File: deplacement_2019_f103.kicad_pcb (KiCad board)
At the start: 2 copper layers, 67.3 x 80 mm, 17 parts, among them J1 alim_logique_5V, J2 moteur_droit, J3 moteur_gauche, J4 Conn_01x03, J5 QEI_droite, J6 QEI_gauche, U1 black_pill

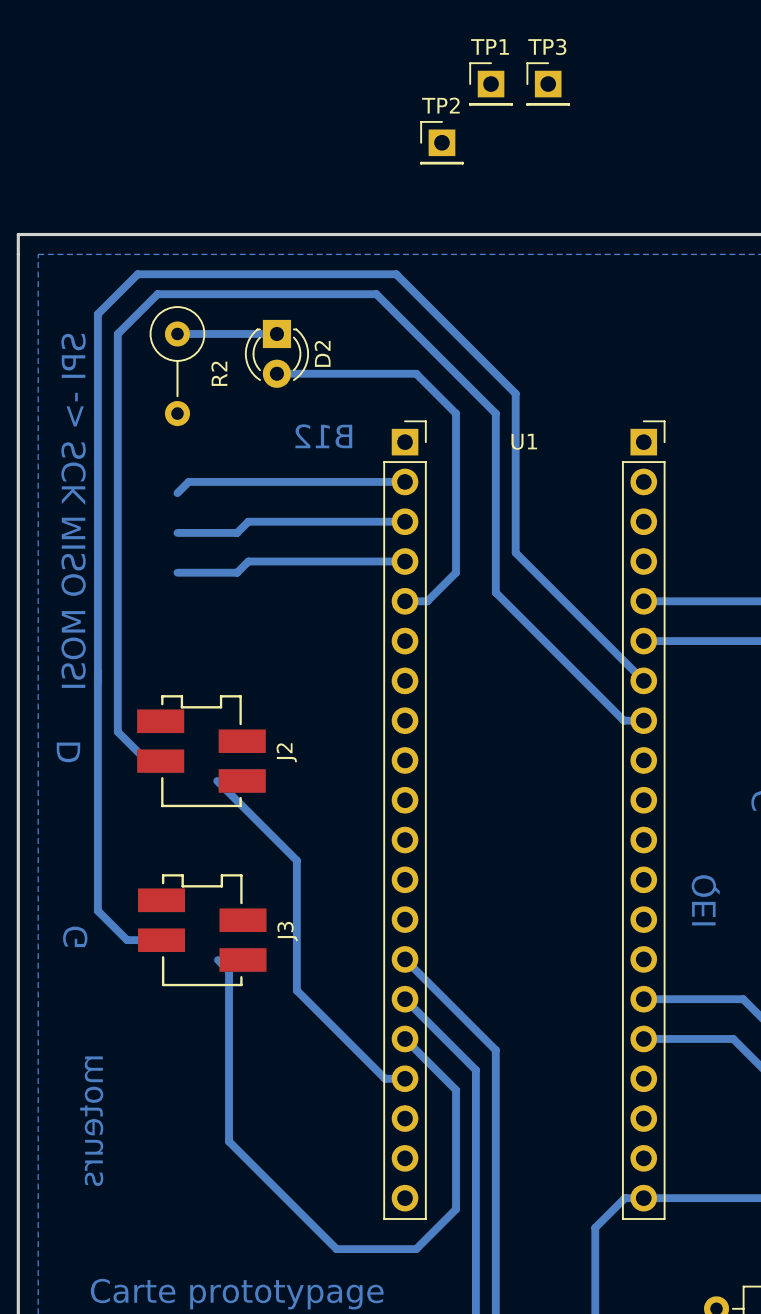
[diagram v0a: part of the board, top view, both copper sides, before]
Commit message: Fix invalid PCB.
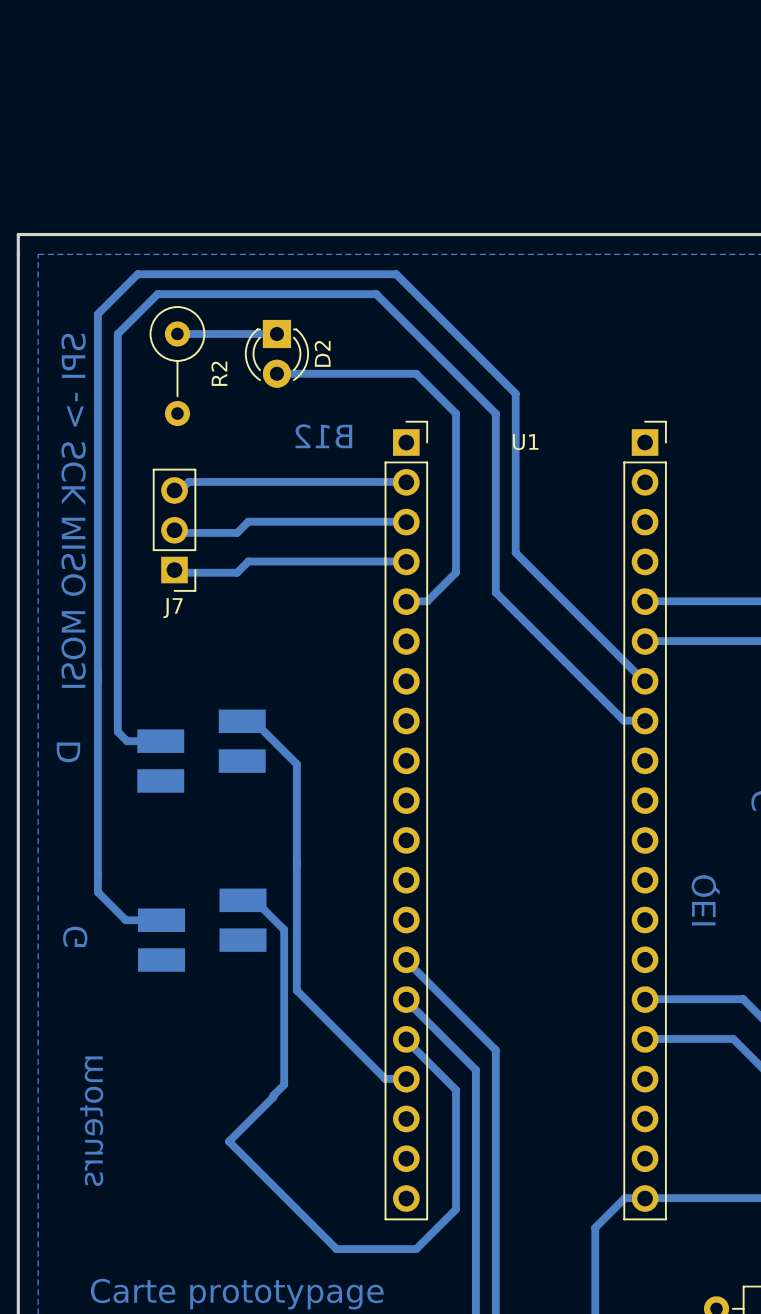
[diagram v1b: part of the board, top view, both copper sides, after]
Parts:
- removed TP1, TP2, TP3: TestPoint, Connector_PinHeader_2.54mm:PinHeader_1x01_P2.54mm_Vertical
- added J7: Conn_01x03_Male, Connector_PinHeader_2.54mm:PinHeader_1x03_P2.54mm_Vertical, F.Cu at (97.6, 67.1)
- J2, J3: moved to B.Cu
- moved U1 0.09 mm to (112.4, 59.0)
- turned J2 to 90 degrees
- turned J3 to 90 degrees
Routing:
- net Direction_moteur_gauche: track 42.5 -> 49.0 mm
- net Direction_moteur_droit: track 24.7 -> 28.6 mm
- net PWM_moteur_gauche: track 97.2 -> 94.9 mm
- net PWM_moteur_droit: track 82.6 -> 81.0 mm

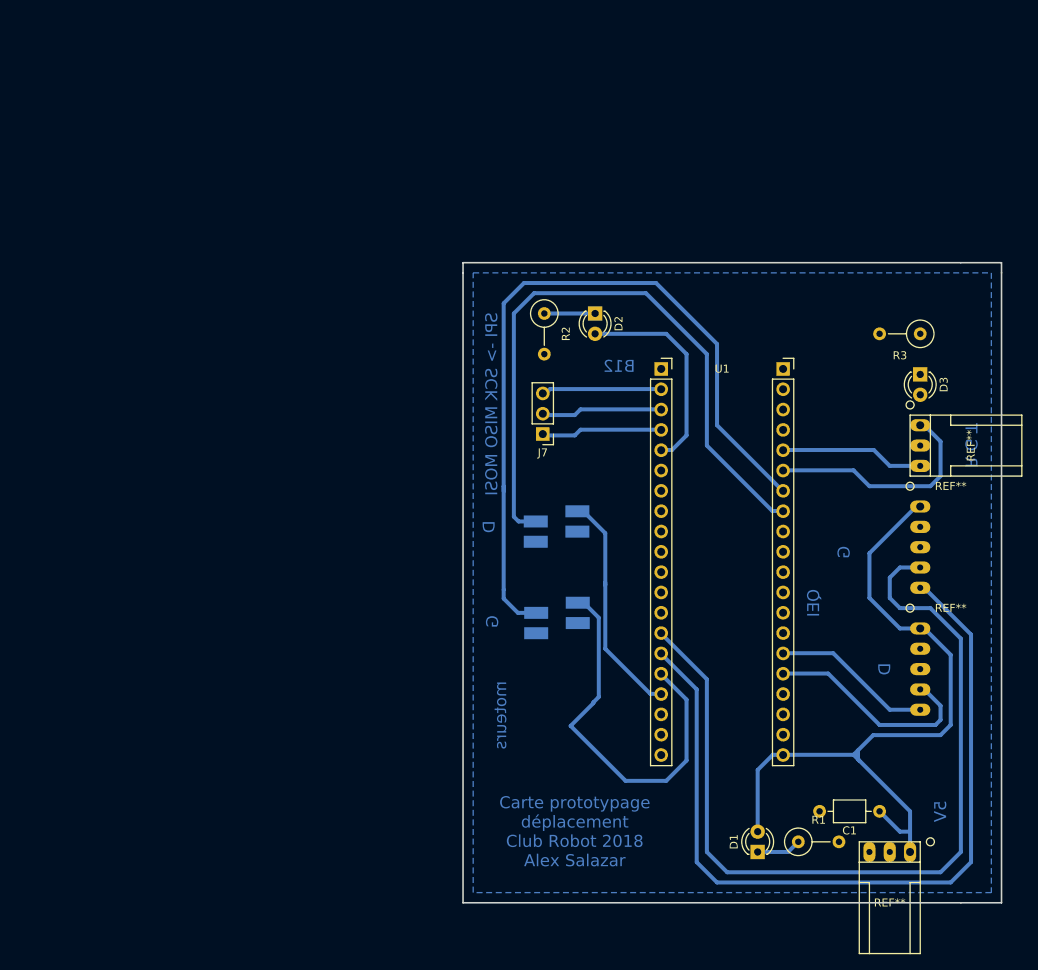
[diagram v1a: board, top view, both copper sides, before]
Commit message: added ethernet connector
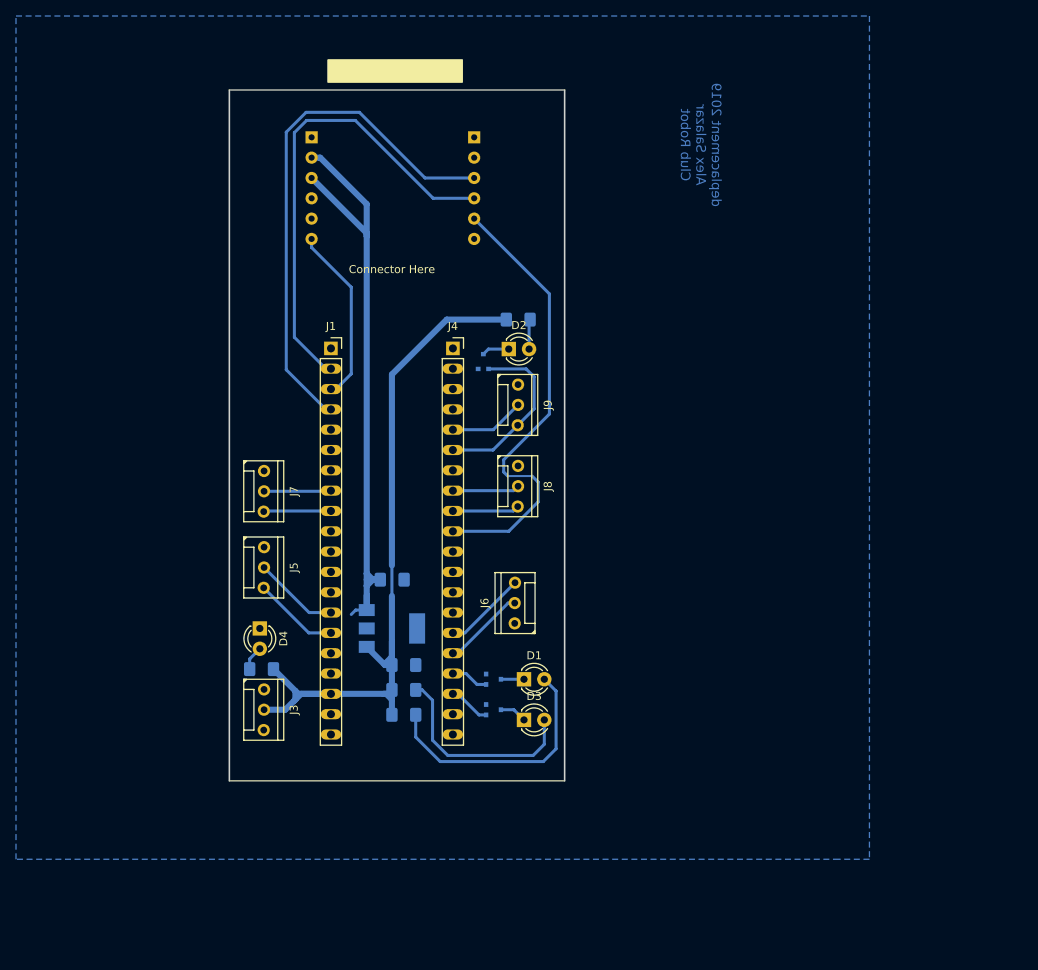
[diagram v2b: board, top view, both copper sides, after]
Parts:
- removed J2: moteur_droit, @Robot:ConnectorMicromatch-4
- removed R2, R3: R, Resistor_THT:R_Axial_DIN0309_L9.0mm_D3.2mm_P5.08mm_Vertical
- added C2: 1u, Capacitor_SMD:C_1206_3216Metric_Pad1.42x1.75mm_HandSolder, B.Cu at (78.8, 85.3)
- added D4: LED_alimentation_rouge, LED_THT:LED_D3.0mm, F.Cu at (62.2, 91.4)
- added J8: PWM output, @Robot:HE14-3-straight, F.Cu at (95.2, 73.7)
- added J9: Liaison serie, @Robot:HE14-3-straight, F.Cu at (95.2, 63.5)
- added Q1: PMF370XN, digikey-footprints:SOT-323, B.Cu at (91.4, 97.8)
- added Q3: PMF370XN, digikey-footprints:SOT-323, B.Cu at (90.2, 58.1)
- added Q4: PMF370XN, digikey-footprints:SOT-323, B.Cu at (91.4, 101.6)
- added R4: 150, Resistor_SMD:R_1206_3216Metric_Pad1.42x1.75mm_HandSolder, B.Cu at (94.5, 52.8)
- added R5: 150, Resistor_SMD:R_1206_3216Metric_Pad1.42x1.75mm_HandSolder, B.Cu at (80.2, 99.1)
- added R6: 150, Resistor_SMD:R_1206_3216Metric_Pad1.42x1.75mm_HandSolder, B.Cu at (62.4, 96.5)
- added U2: w5500, @Robot:w5500, B.Cu at (78.7, 35.6)
- C1: value C -> 1u; footprint Capacitor_THT:C_Axial_L3.8mm_D2.6mm_P7.50mm_Horizontal -> Capacitor_SMD:C_1206_3216Metric_Pad1.42x1.75mm_HandSolder; moved to B.Cu
- D1: value LED -> LED_hardfault_jaune
- D2: value LED -> LED_communication_vert
- D3: value LED -> LED_ucontrolleur_vert
- J1: value alim_logique_5V -> Conn_01x20_Female; footprint @Robot:HE14-3_horizontal -> @Robot:PinSocket_1x20_P2.54mm_Vertical_Long_Pads
- J3: value moteur_gauche -> Alim logique; footprint @Robot:ConnectorMicromatch-4 -> @Robot:HE14-3-straight; moved to F.Cu
- J4: value Conn_01x03 -> Conn_01x20_Female; footprint @Robot:HE14-3_horizontal -> @Robot:PinSocket_1x20_P2.54mm_Vertical_Long_Pads
- J5: value QEI_droite -> PWM input; footprint @Robot:HE14-5_horizontal -> @Robot:HE14-3-straight
- J6: value QEI_gauche -> PWM input; footprint @Robot:HE14-5_horizontal -> @Robot:HE14-3-straight
- J7: value Conn_01x03_Male -> PWM output; footprint Connector_PinHeader_2.54mm:PinHeader_1x03_P2.54mm_Vertical -> @Robot:HE14-3-straight
- R1: value R -> 150; footprint Resistor_THT:R_Axial_DIN0309_L9.0mm_D3.2mm_P5.08mm_Vertical -> Resistor_SMD:R_1206_3216Metric_Pad1.42x1.75mm_HandSolder; moved to B.Cu
- U1: value black_pill -> TC1262-33; footprint @Robot:black_pill -> Package_TO_SOT_SMD:SOT-223-3_TabPin2; moved to B.Cu
- moved J1 96.6 mm to (71.1, 56.4), turned to 0 degrees
- moved J5 85.7 mm to (63.5, 83.8)
- moved D3 65.7 mm to (95.2, 102.9), turned to 0 degrees
- moved J4 63.4 mm to (86.4, 56.4), turned to 0 degrees
- moved C1 62.2 mm to (80.2, 96.0), turned to 0 degrees
- moved J6 56.1 mm to (93.3, 88.3), turned to 90 degrees
- moved R1 51.8 mm to (80.2, 102.2)
- moved U1 46.7 mm to (78.7, 91.4)
- moved J3 37.4 mm to (63.5, 101.6), turned to 270 degrees
- moved D1 36.3 mm to (95.2, 97.8), turned to 0 degrees
- moved J7 34.8 mm to (63.5, 74.3), turned to 270 degrees
- moved D2 11.7 mm to (93.3, 56.5), turned to 0 degrees
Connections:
- D1 pad 2: +5V -> Net-(D1-Pad2)
- D2 pad 2: LED_feedback -> Net-(D2-Pad2)
- D3 pad 2: LED_TX -> Net-(D3-Pad2)
- J1 pad 1: +5V -> Net-(J1-Pad1)
- J1 pad 2: GND -> /SCLK
- J1 pad 3: Net-(J1-Pad3) -> /MISO
- J3 pad 1: Direction_moteur_gauche -> GND
- J3 pad 2: PWM_moteur_gauche -> +5V
- J3 pad 3: GND -> Net-(J3-Pad3)
- J4 pad 1: LED_TX -> GND
- J4 pad 3: RX -> Net-(J4-Pad3)
- J5 pad 1: +5V -> GND
- J5 pad 2: GND -> /qei_left_A
- J5 pad 3: Net-(J5-Pad3) -> /qei_left_B
- J6 pad 1: +5V -> GND
- J6 pad 2: GND -> /qei_right_A
- J6 pad 3: Net-(J6-Pad3) -> /qei_right_B
- J7 pad 1: SPI_MOSI -> GND
- J7 pad 2: SPI_MISO -> /motor_left_PWM
- J7 pad 3: SPI_SCK -> /motor_left_direction
- R1 pad 1: Net-(D1-Pad1) -> +5V
- R1 pad 2: GND -> Net-(D1-Pad2)
- U1 pad 1: Net-(U1-Pad1) -> +5V
- U1 pad 2: SPI_SCK -> GND
- U1 pad 3: SPI_MISO -> +3V3
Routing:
- net QEI_gauche_1: track 108.7 -> 0.00 mm
- net QEI_gauche_2: track 101.6 -> 0.00 mm
- net PWM_moteur_gauche: track 94.9 -> 0.00 mm
- net PWM_moteur_droit: track 81.0 -> 0.00 mm
- net +3V3: track 0.00 -> 79.5 mm
- net /MOSI: track 0.00 -> 65.3 mm
- net /SCLK: track 0.00 -> 58.9 mm
- net /CS: track 0.00 -> 57.4 mm
- net Direction_moteur_gauche: track 49.0 -> 0.00 mm
- net Net-(D1-Pad2): track 0.00 -> 31.6 mm
- net LED_TX: track 28.8 -> 0.00 mm
- net Direction_moteur_droit: track 28.6 -> 0.00 mm
- net QEI_droite_1: track 27.9 -> 0.00 mm
- net LED_feedback: track 26.7 -> 0.00 mm
- net Net-(D3-Pad2): track 0.00 -> 26.0 mm
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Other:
- board size 67.3 x 80 mm -> 41.9 x 86.4 mm
- net class Default: clearance 0.2 -> 0.381; trace_width 0.5 -> 0.762
- net class Interpin removed
- rule trace_clearance: 0.2 -> 0.381
- board text added: "deplacement 2019 Alex Salazar Club Robot"
- board text removed: "1"
- board text removed: "1 novembre 2018"
- board text removed: "5V"
- board text removed: "B12"
- board text removed: "Carte proto déplacement"
- board text removed: "Carte prototypage déplacement Club Robot 2018 Alex Salazar"
- board text removed: "D"
- board text removed: "G"
- board text removed: "QEI"
- board text removed: "R G T"
- board text removed: "SPI -> SCK MISO MOSI"
- board text removed: "moteurs"

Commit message: fixed routing mistake
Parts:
- added REF**: MountingHole_3.2mm_M3, MountingHole:MountingHole_3.2mm_M3, F.Cu at (76.5, 107.2)
- added REF**: MountingHole_3.2mm_M3, MountingHole:MountingHole_3.2mm_M3, F.Cu at (97.5, 81.0)
- added REF**: MountingHole_3.2mm_M3, MountingHole:MountingHole_3.2mm_M3, F.Cu at (61.7, 27.4)
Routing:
- net +3V3: track 79.5 -> 77.3 mm

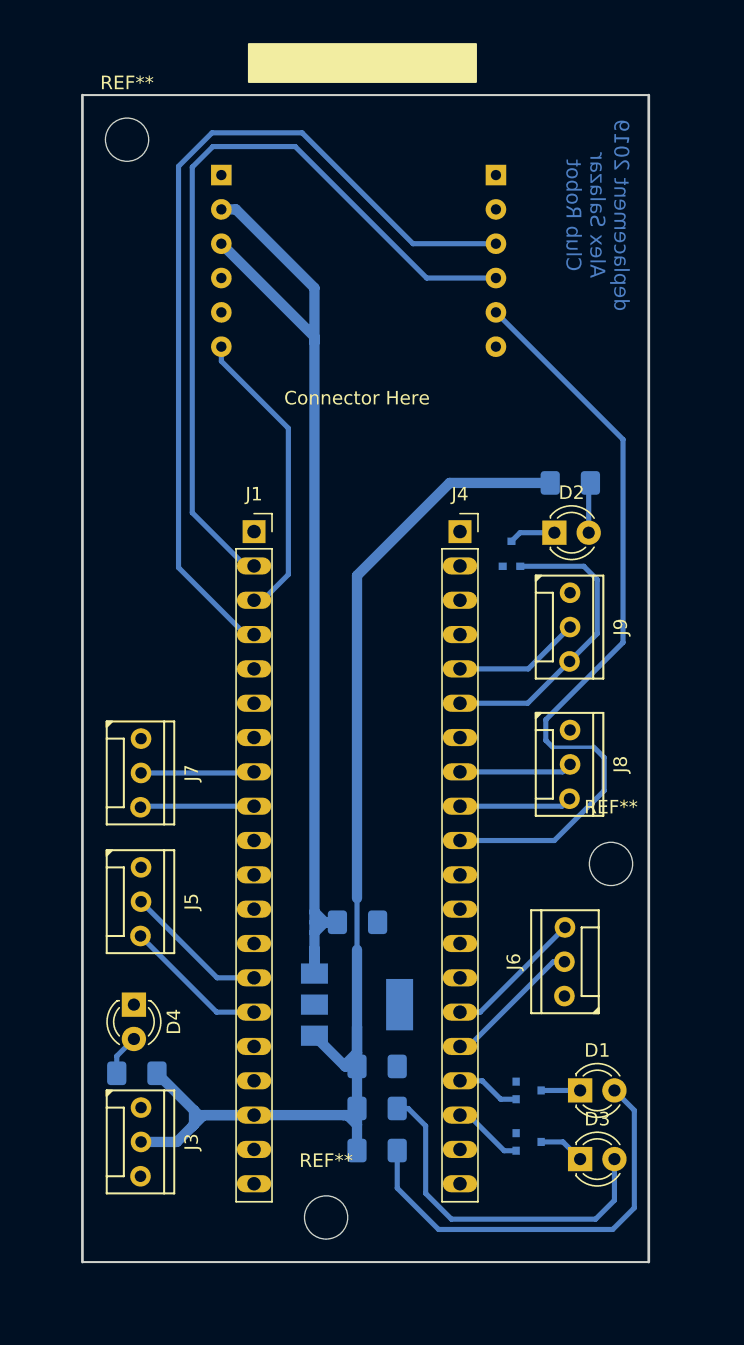
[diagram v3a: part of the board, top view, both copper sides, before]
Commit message: Integrate w5500 change
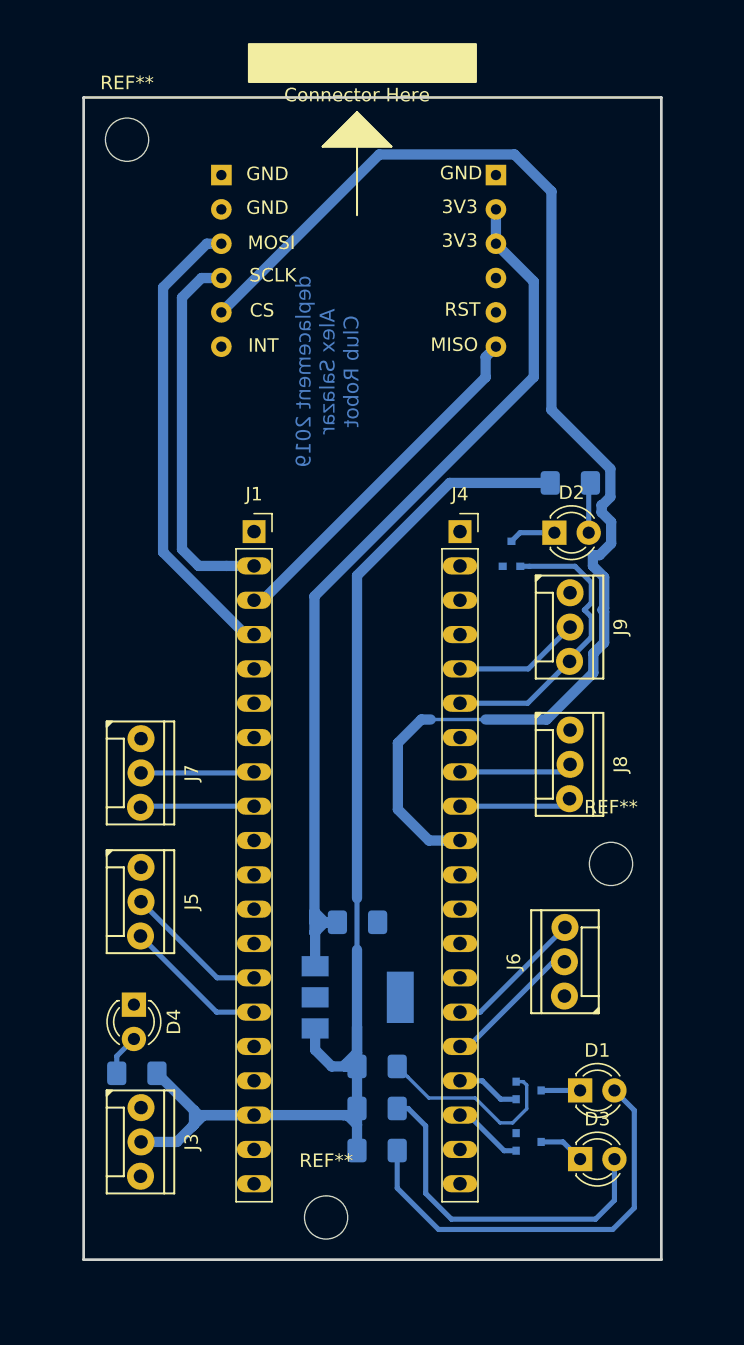
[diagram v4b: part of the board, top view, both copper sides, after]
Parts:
- U2: moved to F.Cu
- moved U1 0.54 mm to (78.8, 90.9)
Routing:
- net /CS: track 57.4 -> 97.1 mm
- net /MOSI: track 65.3 -> 34.5 mm
- net /SCLK: track 58.9 -> 28.6 mm
- net GND: track 0.00 -> 14.4 mm
- net +3V3: track 77.3 -> 69.8 mm
- net /MISO: track 22.2 -> 26.6 mm
- net +5V: track 97.7 -> 99.7 mm
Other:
- board size 41.9 x 86.4 mm -> 42.8 x 86 mm

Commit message: Updated the entire PCB to the previous w5500 change
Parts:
- removed J9: Liaison serie, @Robot:HE14-3-straight
- removed Q4: PMF370XN, digikey-footprints:SOT-323
- removed R5, R6: 150, Resistor_SMD:R_1206_3216Metric_Pad1.42x1.75mm_HandSolder
- removed REF** (x3): MountingHole_3.2mm_M3, MountingHole:MountingHole_3.2mm_M3
- added C3: 100uF, Capacitor_THT:CP_Radial_D5.0mm_P2.50mm, F.Cu at (149.8, 121.9)
- added J2: Connecteur Gauche, @Robot:PinSocket_1x20_P2.54mm_Vertical_Long_Pads, F.Cu at (141.5, 75.5)
- added Q2: PMF370XN, Package_TO_SOT_SMD:SOT-323_SC-70_Handsoldering, B.Cu at (165.1, 86.4)
- added R2: 150, Resistor_SMD:R_1206_3216Metric_Pad1.42x1.75mm_HandSolder, B.Cu at (168.9, 98.0)
- added R3: 150, Resistor_SMD:R_1206_3216Metric_Pad1.42x1.75mm_HandSolder, B.Cu at (174.2, 120.7)
- J1: value Conn_01x20_Female -> Alim logique; footprint @Robot:PinSocket_1x20_P2.54mm_Vertical_Long_Pads -> @Robot:HE14-3-straight
- J3: value Alim logique -> Connecteur Droit; footprint @Robot:HE14-3-straight -> @Robot:PinSocket_1x20_P2.54mm_Vertical_Long_Pads
- J4: value Conn_01x20_Female -> Conn_01x05; footprint @Robot:PinSocket_1x20_P2.54mm_Vertical_Long_Pads -> @Robot:HE14-5_horizontal
- J5: value PWM input -> Conn_01x05; footprint @Robot:HE14-3-straight -> @Robot:HE14-5_horizontal
- J6: value PWM input -> PWM output
- J8: value PWM output -> Liaison serie
- Q1, Q3: footprint digikey-footprints:SOT-323 -> Package_TO_SOT_SMD:SOT-323_SC-70_Handsoldering
- moved J5 107.1 mm to (168.7, 104.1)
- moved J1 106.1 mm to (149.9, 127.5)
- moved J7 104.5 mm to (166.4, 92.7)
- moved J3 96.9 mm to (156.8, 75.5), turned to 0 degrees
- moved Q3 95.3 mm to (162.6, 120.0), turned to 0 degrees
- moved R1 94.9 mm to (174.2, 115.6), turned to 180 degrees
- moved R4 89.1 mm to (142.0, 128.3), turned to 180 degrees
- moved D4 81.3 mm to (135.9, 125.7)
- moved D2 81.2 mm to (168.9, 86.4)
- moved C2 80.4 mm to (154.9, 59.5), turned to 270 degrees
- moved U1 77.6 mm to (149.9, 59.7), turned to 270 degrees
- moved D1 74.7 mm to (167.6, 116.2)
- moved D3 74.5 mm to (167.6, 120.7)
- moved C1 73.9 mm to (144.6, 59.7), turned to 180 degrees
- moved U2 73.5 mm to (148.6, 58.4)
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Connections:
- J1 pad 1: Net-(J1-Pad1) -> GND
- J1 pad 2: /SCLK -> +5V
- J1 pad 3: /MISO -> Net-(J1-Pad3)
- J3 pad 2: +5V -> GND
- J4 pad 2: GND -> +5V
- J4 pad 3: Net-(J4-Pad3) -> /qei_left_A
- J4 pad 4: Net-(J4-Pad4) -> /qei_left_B
- J4 pad 5: /RX -> Net-(J4-Pad5)
- J5 pad 2: /qei_left_A -> +5V
- J5 pad 3: /qei_left_B -> /qei_right_A
- J6 pad 2: /qei_right_A -> /motor_left_PWM
- J6 pad 3: /qei_right_B -> /motor_left_direction
- J7 pad 2: /motor_left_PWM -> /motor_right_PWM
- J7 pad 3: /motor_left_direction -> /motor_right_direction
- J8 pad 2: /motor_right_PWM -> /RX
- J8 pad 3: /motor_right_direction -> /TX
- Q3 pad 1: /TX -> /led_feedback
- Q3 pad 3: Net-(D2-Pad1) -> Net-(D3-Pad1)
- R4 pad 2: Net-(D2-Pad2) -> Net-(D4-Pad2)
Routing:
- net /CS: track 97.1 -> 26.8 mm
- net +3V3: track 69.8 -> 12.3 mm
- net +5V: track 99.7 -> 154.3 mm, vias 0 -> 2
- net /MISO: track 26.6 -> 79.0 mm
- net Net-(D1-Pad2): track 31.6 -> 2.80 mm
- net Net-(D3-Pad2): track 26.0 -> 2.54 mm
- net /qei_left_A: track 10.7 -> 31.9 mm
- net /SCLK: track 28.6 -> 47.4 mm
- net GND: track 14.4 -> 25.4 mm, vias 0 -> 1
- net /TX: track 22.1 -> 11.7 mm
- net /led_communication: track 0.00 -> 9.12 mm
- net Net-(D2-Pad2): track 3.74 -> 11.2 mm
- net /qei_right_A: track 10.3 -> 17.5 mm
- net /MOSI: track 34.5 -> 29.7 mm
- net /qei_left_B: track 10.7 -> 14.5 mm
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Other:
- board size 42.8 x 86 mm -> 50.8 x 85.1 mm
- net class Default: via_dia 0.8 -> 1.5; via_drill 0.4 -> 0.8
- board text added: "Carte deplacement Alex Salazar 2019 Club Robot"
- board text removed: "deplacement 2019 Alex Salazar Club Robot"
